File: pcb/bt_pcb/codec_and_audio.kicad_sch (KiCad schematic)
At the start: 10 parts, among them U1 CS4272

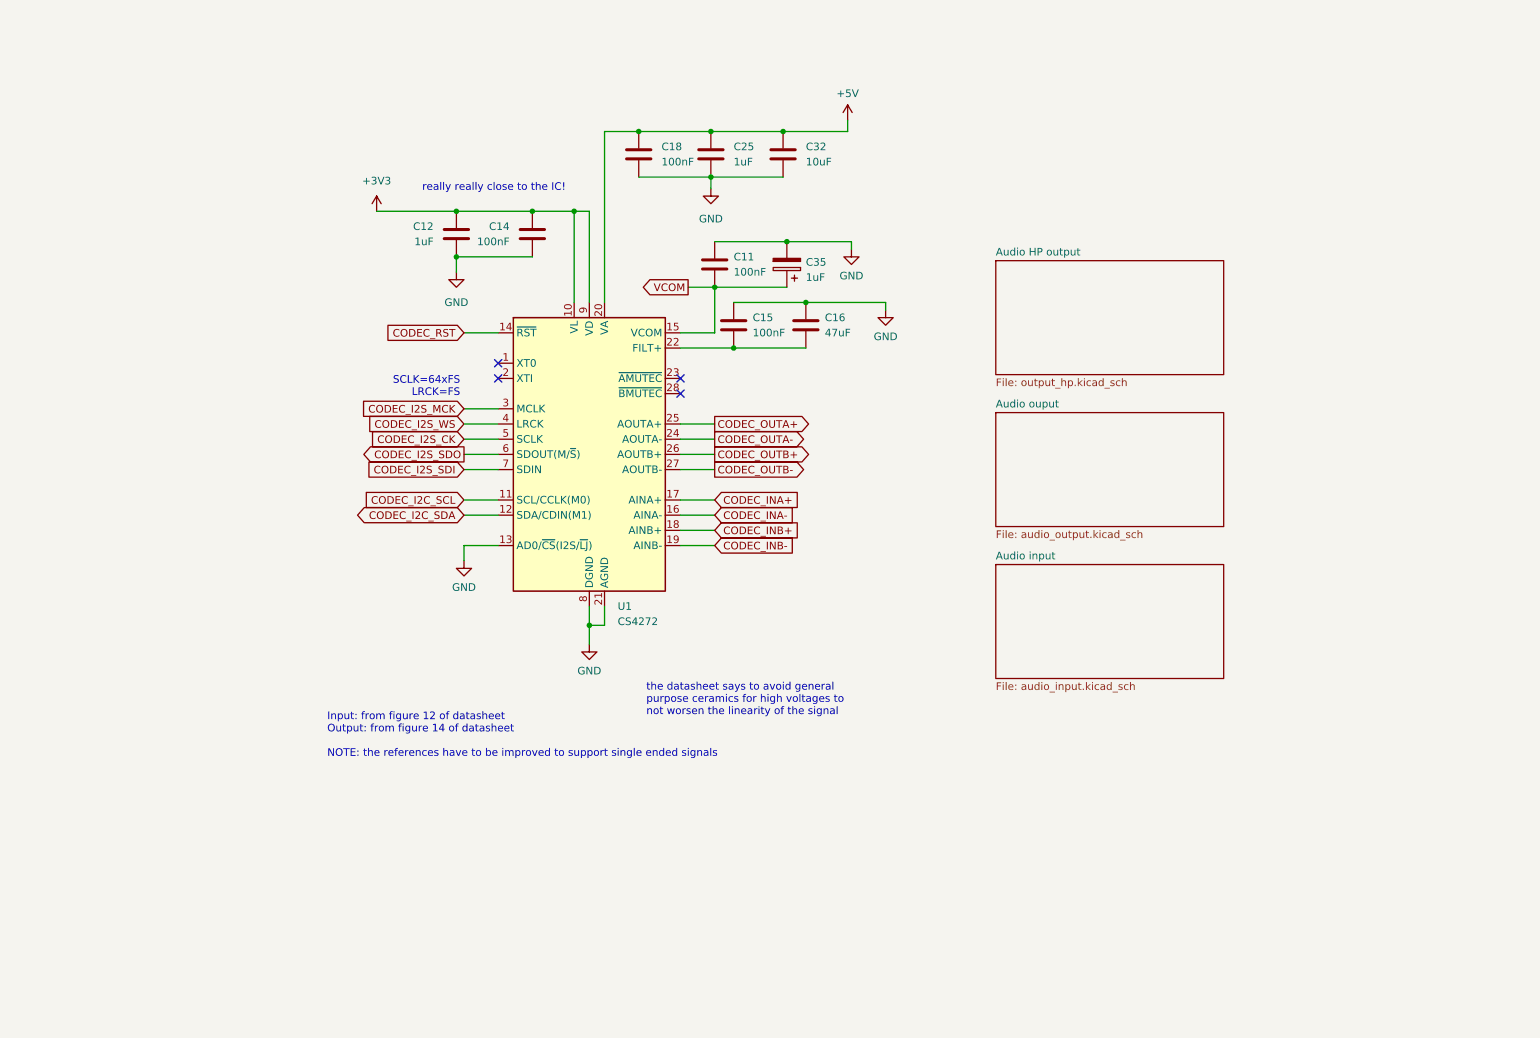
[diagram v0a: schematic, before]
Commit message: ditching power pcb, new codec
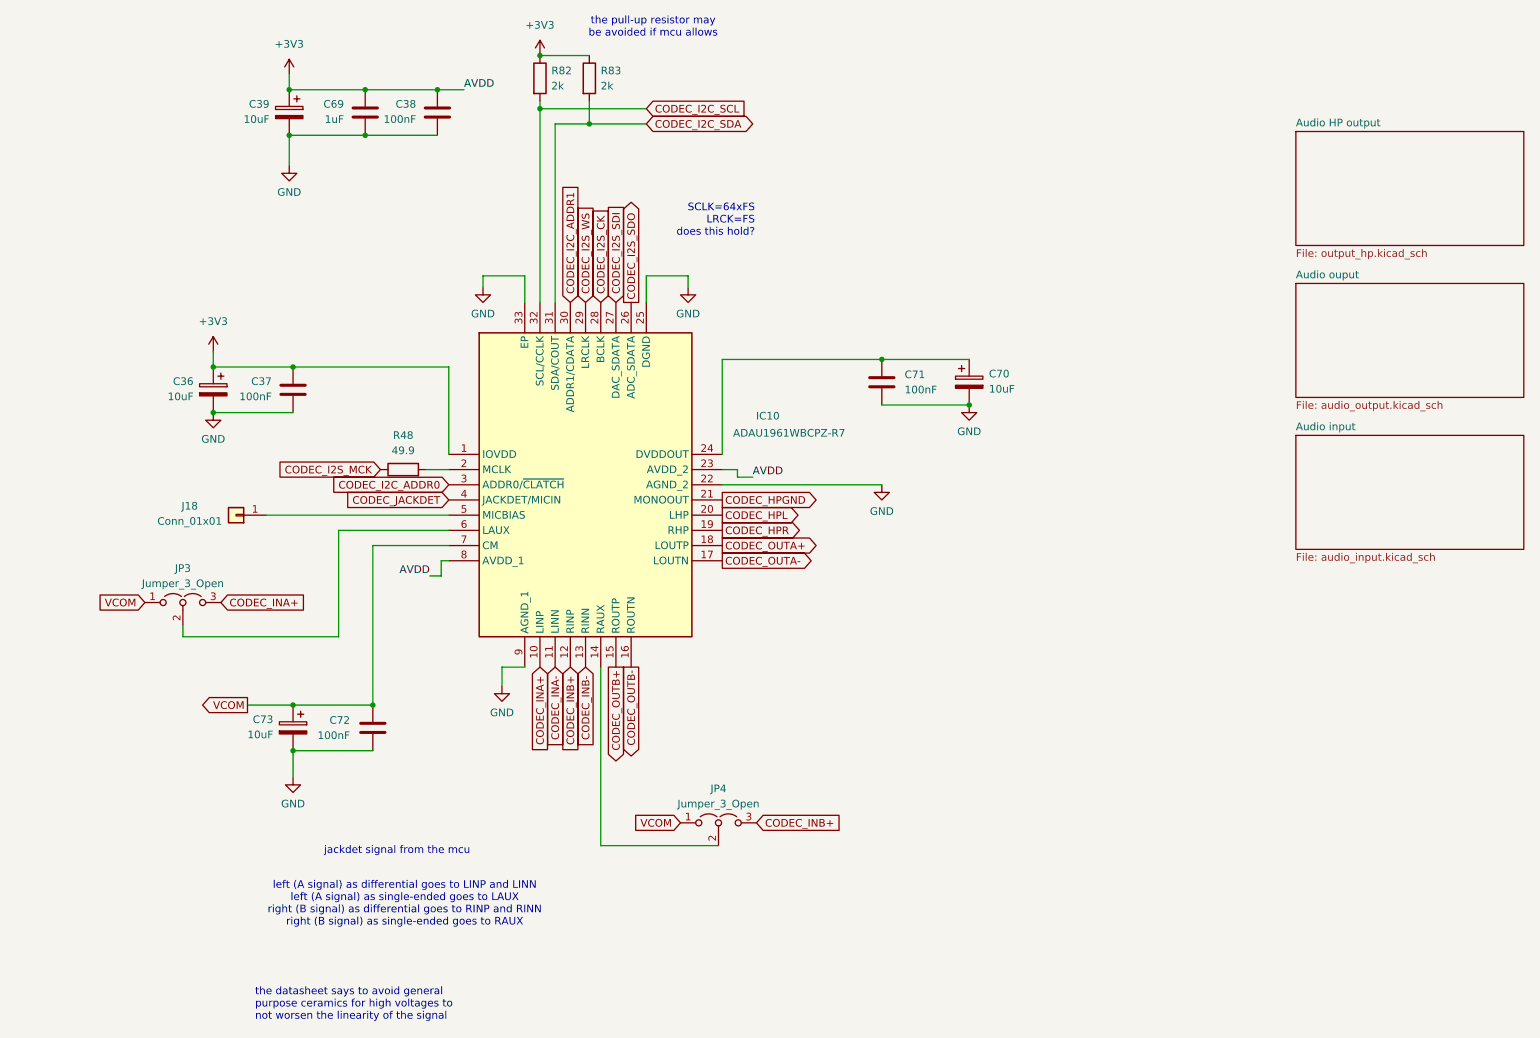
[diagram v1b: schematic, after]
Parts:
- removed C11, C14, C15, C18: 100nF, symbol Device:C
- removed C12, C25: 1uF, symbol Device:C
- removed C16: 47uF, symbol Device:C
- removed C32: 10uF, symbol Device:C
- removed C35: 1uF, symbol Device:C_Polarized
- removed U1: CS4272, Package_SO:TSSOP-28_4.4x9.7mm_P0.65mm, symbol Audio:CS4272
- added C36, C39, C70, C73: 10uF, symbol Device:C_Polarized
- added C37, C38, C71, C72: 100nF, symbol Device:C
- added C69: 1uF, symbol Device:C
- added IC10: ADAU1961WBCPZ-R7, QFN50P500X500X100-33N-D, symbol library:ADAU1961WBCPZ-R7
- added J18: Conn_01x01, symbol Connector_Generic:Conn_01x01
- added JP3, JP4: Jumper_3_Open, symbol Jumper:Jumper_3_Open
- added R48: 49.9, symbol Device:R
- added R82, R83: 2k, symbol Device:R
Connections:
- net +3V3: now also C36.1, C37.1, C38.1, C39.1, C69.1, IC10.1 (IOVDD), IC10.23 (AVDD_2), IC10.8 (AVDD_1), R82.1, R83.1
- net CODEC_I2C_SCL: now also IC10.32 (SCL/CCLK), R82.2
- net CODEC_I2C_SDA: now also IC10.31 (SDA/COUT), R83.2
- net CODEC_I2S_CK: now also IC10.28 (BCLK)
- net CODEC_I2S_MCK: now also R48.1
- net CODEC_I2S_SDI: now also IC10.27 (DAC_SDATA)
- net CODEC_I2S_SDO: now also IC10.26 (ADC_SDATA)
- net CODEC_I2S_WS: now also IC10.29 (LRCLK)
- net CODEC_INA+: now also IC10.10 (LINP), JP3.3 (B)
- net CODEC_INA-: now also IC10.11 (LINN)
- net CODEC_INB+: now also IC10.12 (RINP), JP4.3 (B)
- net CODEC_INB-: now also IC10.13 (RINN)
- net CODEC_OUTA+: now also IC10.18 (LOUTP)
- net CODEC_OUTA-: now also IC10.17 (LOUTN)
- net CODEC_OUTB+: now also IC10.15 (ROUTP)
- net CODEC_OUTB-: now also IC10.16 (ROUTN)
- net GND: now also C36.2, C37.2, C38.2, C39.2, C69.2, C70.2, C71.2, C72.2, C73.2, IC10.22 (AGND_2), IC10.25 (DGND), IC10.33 (EP), IC10.9 (AGND_1)
- net VCOM: now also C72.1, C73.1, IC10.7 (CM), JP3.1 (A), JP4.1 (A)
- new net: IC10.2 (MCLK), R48.2
- new net: IC10.14 (RAUX), JP4.2 (C)
- new net: C70.1, C71.1, IC10.24 (DVDDOUT)
- new net: IC10.5 (MICBIAS), J18.1 (Pin_1)
- new net: IC10.6 (LAUX), JP3.2 (C)
- new net CODEC_HPGND: IC10.21 (MONOOUT)
- new net CODEC_HPL: IC10.20 (LHP)
- new net CODEC_HPR: IC10.19 (RHP)
- new net CODEC_I2C_ADDR0: IC10.3 (ADDR0/~{CLATCH})
- new net CODEC_I2C_ADDR1: IC10.30 (ADDR1/CDATA)
- new net CODEC_JACKDET: IC10.4 (JACKDET/MICIN)
- no-connect marks 4 -> 0
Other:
- note added: "SCLK=64xFS LRCK=FS does this hold?"
- note added: "jackdet signal from the mcu"
- note added: "left (A signal) as differential goes to LINP and LINN left (A signal) as single-ended goes to LAUX right (B signal) as differential goes to RINP and RINN right (B signal) as single-ended goes to RAUX"
- note added: "the pull-up resistor may be avoided if mcu allows"
- note removed: "Input: from figure 12 of datasheet Output: from figure 14 of datasheet NOTE: the references have to be improved to support single ended signals"
- note removed: "SCLK=64xFS LRCK=FS"
- note removed: "really really close to the IC!"

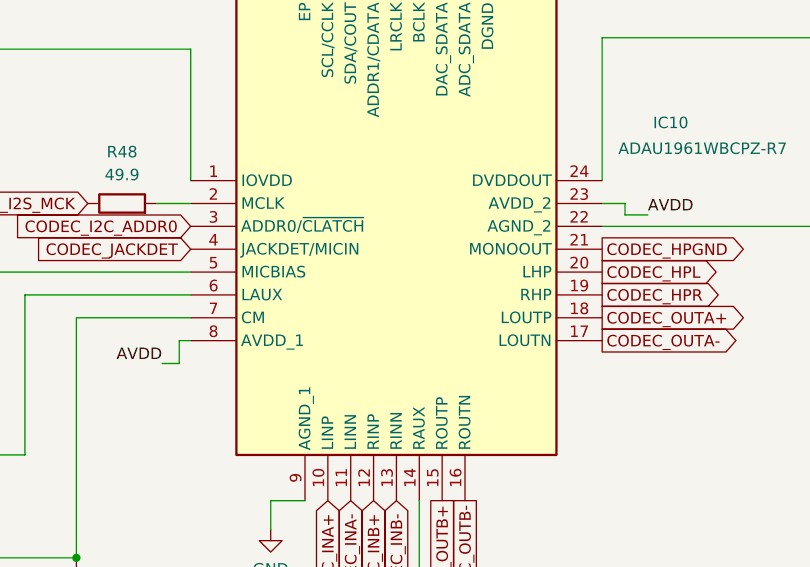
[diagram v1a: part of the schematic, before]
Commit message: complete makeover of power supply
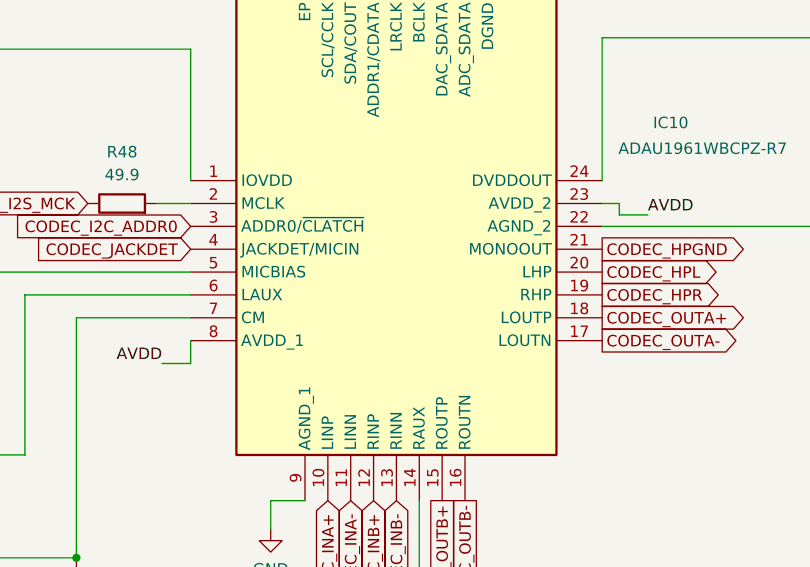
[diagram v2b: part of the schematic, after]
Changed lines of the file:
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@@
 	(wire
 		(pts
-			(xy 98.425 114.3) (xy 100.33 114.3)
+			(xy 98.425 114.3) (xy 101.6 114.3)
 		)
 		(stroke
@@
 	(wire
 		(pts
-			(xy 100.33 114.3) (xy 100.33 111.76)
-		)
-		(stroke
-			(width 0)
-			(type default)
-		)
-	)
-	(wire
-		(pts
-			(xy 100.33 111.76) (xy 101.6 111.76)
+			(xy 101.6 114.3) (xy 101.6 111.76)
 		)
 		(stroke
@@
 	(wire
 		(pts
-			(xy 152.4 97.79) (xy 149.86 97.79)
+			(xy 152.4 97.79) (xy 149.225 97.79)
 		)
 		(stroke
@@
 	(wire
 		(pts
-			(xy 149.86 96.52) (xy 147.32 96.52)
+			(xy 149.225 96.52) (xy 147.32 96.52)
 		)
 		(stroke
@@
 	(wire
 		(pts
-			(xy 149.86 97.79) (xy 149.86 96.52)
-		)
-		(stroke
+			(xy 149.225 97.79) (xy 149.225 96.52)
+		)
+		(stroke

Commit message: big progress, now revising error and warnings
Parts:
- removed C36, C39, C70, C73: 10uF, symbol Device:C_Polarized
- removed R82, R83: 2k, symbol Device:R
- added C3, C4, C5, C6: 10uF, symbol Device:C
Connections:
- net +3V3: now also C5.1; no longer C38.1, C69.1, IC10.23 (AVDD_2), IC10.8 (AVDD_1)
- net GND: now also C3.2, C4.2, C5.2, C6.2
- net VCOM: now also C6.1
- net at C71.1, IC10.24 (DVDDOUT): now also C3.1
- new net +3V3A: C38.1, C4.1, C69.1, IC10.23 (AVDD_2), IC10.8 (AVDD_1)
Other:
- note removed: "the pull-up resistor may be avoided if mcu allows"

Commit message: solving some erc warnings and errors
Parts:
- IC2: renamed from IC10; footprint QFN50P500X500X100-33N-D -> library:QFN50P500X500X100-33N-D
- renumbered C5 to C15, C4 to C16, C37 to C17, C6 to C18, C69 to C19, C72 to C20, C38 to C21, C71 to C22, C3 to C23, J18 to J3, JP3 to JP1, JP4 to JP2, R48 to R2
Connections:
- net +3V3A renamed +3.3VA
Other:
- moved on the sheet: C15, C17, C18, C21, C22, C23, JP1, JP2

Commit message: schematic in theory finished
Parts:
- removed JP1, JP2: Jumper_3_Open, symbol Jumper:Jumper_3_Open
- added J4: Conn_01x03, Connector_PinHeader_2.54mm:PinHeader_1x01_P2.54mm_Vertical, symbol Connector_Generic:Conn_01x03
- added R3, R4, R5, R6: 0, Resistor_SMD:R_0603_1608Metric_Pad0.98x0.95mm_HandSolder, symbol Device:R
- C15: renamed from C16; value 10uF -> 10u; footprint (none) -> Capacitor_SMD:C_0805_2012Metric_Pad1.18x1.45mm_HandSolder
- C16: renamed from C19; value 1uF -> 1u; footprint (none) -> Capacitor_SMD:C_0603_1608Metric_Pad1.08x0.95mm_HandSolder
- C17: renamed from C21; value 100nF -> 100n; footprint (none) -> Capacitor_SMD:C_0603_1608Metric_Pad1.08x0.95mm_HandSolder
- C18: renamed from C22; value 100nF -> 100n; footprint (none) -> Capacitor_SMD:C_0603_1608Metric_Pad1.08x0.95mm_HandSolder
- C19: renamed from C23; value 10uF -> 10u; footprint (none) -> Capacitor_SMD:C_0805_2012Metric_Pad1.18x1.45mm_HandSolder
- C20: renamed from C15; value 10uF -> 10u; footprint (none) -> Capacitor_SMD:C_0805_2012Metric_Pad1.18x1.45mm_HandSolder
- C21: renamed from C17; value 100nF -> 100n; footprint (none) -> Capacitor_SMD:C_0603_1608Metric_Pad1.08x0.95mm_HandSolder
- C22: renamed from C18; value 10uF -> 10u; footprint (none) -> Capacitor_SMD:C_0805_2012Metric_Pad1.18x1.45mm_HandSolder
- C23: renamed from C20; value 100nF -> 100n; footprint (none) -> Capacitor_SMD:C_0603_1608Metric_Pad1.08x0.95mm_HandSolder
- J3: footprint (none) -> Connector_PinHeader_2.54mm:PinHeader_1x01_P2.54mm_Vertical
- R2: footprint (none) -> Resistor_SMD:R_0603_1608Metric_Pad0.98x0.95mm_HandSolder
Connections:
- net CODEC_HPGND: now also J4.3 (Pin_3)
- net CODEC_HPL: now also J4.1 (Pin_1)
- net CODEC_HPR: now also J4.2 (Pin_2)
- net CODEC_INA+: now also R4.2
- net CODEC_INB+: now also R6.2
- net VCOM: now also R3.1, R5.1
- net at IC2.14 (RAUX): now also R5.2, R6.1
- net at IC2.6 (LAUX): now also R3.2, R4.1
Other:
- removed sheet Audio HP output
- note added: "HEADPHONE OUT Left -> 1 -> T Right -> 2 -> R Ggn -> 3 -> S"

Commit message: pcb started
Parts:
- J5: renamed from J4; footprint Connector_PinHeader_2.54mm:PinHeader_1x01_P2.54mm_Vertical -> Connector_PinHeader_2.54mm:PinHeader_1x03_P2.54mm_Vertical
- renumbered J3 to J4, R2 to R3, R3 to R4, R4 to R5, R5 to R6, R6 to R7
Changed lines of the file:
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@@
 		(dnp no)
 		(fields_autoplaced yes)
-		(property "Reference" "#PWR018"
+		(property "Reference" "#PWR019"
 			(at 62.23 81.28 0)
 			(effects
@@
 			(project ""
 				(path "/eb787481-08cd-41a4-a128-173fa6227c32/4ada0139-8712-47ce-9d4c-ab8fef312f7b"
-					(reference "#PWR018")
+					(reference "#PWR019")
 					(unit 1)
 				)
@@
 		(dnp no)
 		(fields_autoplaced yes)
-		(property "Reference" "#PWR016"
+		(property "Reference" "#PWR017"
 			(at 107.95 72.39 0)
 			(effects
@@
 			(project "bt_pcb"
 				(path "/eb787481-08cd-41a4-a128-173fa6227c32/4ada0139-8712-47ce-9d4c-ab8fef312f7b"
-					(reference "#PWR016")
+					(reference "#PWR017")
 					(unit 1)
 				)
@@
 		(dnp no)
 		(fields_autoplaced yes)
-		(property "Reference" "R3"
+		(property "Reference" "R4"
 			(at 53.34 113.665 90)
 			(effects
@@
 			(project "bt_pcb"
 				(path "/eb787481-08cd-41a4-a128-173fa6227c32/4ada0139-8712-47ce-9d4c-ab8fef312f7b"
-					(reference "R3")
+					(reference "R4")
 					(unit 1)
 				)
@@
 		(dnp no)
 		(fields_autoplaced yes)
-		(property "Reference" "R5"
+		(property "Reference" "R6"
 			(at 143.51 150.495 90)
 			(effects
@@
 			(project "bt_pcb"
 				(path "/eb787481-08cd-41a4-a128-173fa6227c32/4ada0139-8712-47ce-9d4c-ab8fef312f7b"
-					(reference "R5")
+					(reference "R6")
 					(unit 1)
 				)
@@
 		(dnp no)
 		(fields_autoplaced yes)
-		(property "Reference" "#PWR019"
+		(property "Reference" "#PWR020"
 			(at 189.23 92.71 0)
 			(effects
@@
 			(project "bt_pcb"
 				(path "/eb787481-08cd-41a4-a128-173fa6227c32/4ada0139-8712-47ce-9d4c-ab8fef312f7b"
-					(reference "#PWR019")
+					(reference "#PWR020")
 					(unit 1)
 				)
@@
 		(dnp no)
 		(fields_autoplaced yes)
-		(property "Reference" "#PWR022"
+		(property "Reference" "#PWR023"
 			(at 110.49 139.7 0)
 			(effects
@@
 			(project "bt_pcb"
 				(path "/eb787481-08cd-41a4-a128-173fa6227c32/4ada0139-8712-47ce-9d4c-ab8fef312f7b"
-					(reference "#PWR022")
+					(reference "#PWR023")
 					(unit 1)
 				)
@@
 		(dnp no)
 		(fields_autoplaced yes)
-		(property "Reference" "R2"
+		(property "Reference" "R3"
 			(at 93.98 90.805 90)
 			(effects
@@
 			(project ""
 				(path "/eb787481-08cd-41a4-a128-173fa6227c32/4ada0139-8712-47ce-9d4c-ab8fef312f7b"
-					(reference "R2")
+					(reference "R3")
 					(unit 1)
 				)
@@
 		(dnp no)
 		(fields_autoplaced yes)
-		(property "Reference" "#PWR020"
+		(property "Reference" "#PWR021"
 			(at 62.23 93.98 0)
 			(effects
@@
 			(project "bt_pcb"
 				(path "/eb787481-08cd-41a4-a128-173fa6227c32/4ada0139-8712-47ce-9d4c-ab8fef312f7b"
-					(reference "#PWR020")
+					(reference "#PWR021")
 					(unit 1)
 				)
@@
 		(dnp no)
 		(fields_autoplaced yes)
-		(property "Reference" "#PWR014"
+		(property "Reference" "#PWR015"
 			(at 74.93 34.29 0)
 			(effects
@@
 			(project ""
 				(path "/eb787481-08cd-41a4-a128-173fa6227c32/4ada0139-8712-47ce-9d4c-ab8fef312f7b"
-					(reference "#PWR014")
+					(reference "#PWR015")
 					(unit 1)
 				)
@@
 		(dnp no)
 		(fields_autoplaced yes)
-		(property "Reference" "#PWR023"
+		(property "Reference" "#PWR024"
 			(at 76.2 154.94 0)
 			(effects
@@
 			(project "bt_pcb"
 				(path "/eb787481-08cd-41a4-a128-173fa6227c32/4ada0139-8712-47ce-9d4c-ab8fef312f7b"
-					(reference "#PWR023")
+					(reference "#PWR024")
 					(unit 1)
 				)
@@
 		(dnp no)
 		(fields_autoplaced yes)
-		(property "Reference" "J4"
+		(property "Reference" "J5"
 			(at 262.255 134.6199 0)
 			(effects
@@
 			)
 		)
-		(property "Footprint" "Connector_PinHeader_2.54mm:PinHeader_1x01_P2.54mm_Vertical"
+		(property "Footprint" "Connector_PinHeader_2.54mm:PinHeader_1x03_P2.54mm_Vertical"
 			(at 259.08 135.89 0)
 			(effects
@@
 			(project "bt_pcb"
 				(path "/eb787481-08cd-41a4-a128-173fa6227c32/4ada0139-8712-47ce-9d4c-ab8fef312f7b"
-					(reference "J4")
+					(reference "J5")
 					(unit 1)
 				)
@@
 		(dnp no)
 		(fields_autoplaced yes)
-		(property "Reference" "R6"
+		(property "Reference" "R7"
 			(at 151.13 150.495 90)
 			(effects
@@
 			(project "bt_pcb"
 				(path "/eb787481-08cd-41a4-a128-173fa6227c32/4ada0139-8712-47ce-9d4c-ab8fef312f7b"
-					(reference "R6")
+					(reference "R7")
 					(unit 1)
 				)
@@
 		(dnp no)
 		(fields_autoplaced yes)
-		(property "Reference" "R4"
+		(property "Reference" "R5"
 			(at 60.96 113.665 90)
 			(effects
@@
 			(project "bt_pcb"
 				(path "/eb787481-08cd-41a4-a128-173fa6227c32/4ada0139-8712-47ce-9d4c-ab8fef312f7b"
-					(reference "R4")
+					(reference "R5")
 					(unit 1)
 				)
@@
 		(dnp no)
 		(fields_autoplaced yes)
-		(property "Reference" "#PWR015"
+		(property "Reference" "#PWR016"
 			(at 74.93 52.07 0)
 			(effects
@@
 			(project "bt_pcb"
 				(path "/eb787481-08cd-41a4-a128-173fa6227c32/4ada0139-8712-47ce-9d4c-ab8fef312f7b"
-					(reference "#PWR015")
+					(reference "#PWR016")
 					(unit 1)
 				)
@@
 		(on_board yes)
 		(dnp no)
-		(property "Reference" "J3"
+		(property "Reference" "J4"
 			(at 58.293 102.616 0)
 			(effects
@@
 			(project "bt_pcb"
 				(path "/eb787481-08cd-41a4-a128-173fa6227c32/4ada0139-8712-47ce-9d4c-ab8fef312f7b"
-					(reference "J3")
+					(reference "J4")
 					(unit 1)
 				)
@@
 		(dnp no)
 		(fields_autoplaced yes)
-		(property "Reference" "#PWR017"
+		(property "Reference" "#PWR018"
 			(at 142.24 72.39 0)
 			(effects
@@
 			(project "bt_pcb"
 				(path "/eb787481-08cd-41a4-a128-173fa6227c32/4ada0139-8712-47ce-9d4c-ab8fef312f7b"
-					(reference "#PWR017")
+					(reference "#PWR018")
 					(unit 1)
 				)
@@
 		(dnp no)
 		(fields_autoplaced yes)
-		(property "Reference" "#PWR021"
+		(property "Reference" "#PWR022"
 			(at 173.99 105.41 0)
 			(effects
@@
 			(project "bt_pcb"
 				(path "/eb787481-08cd-41a4-a128-173fa6227c32/4ada0139-8712-47ce-9d4c-ab8fef312f7b"
-					(reference "#PWR021")
-					(unit 1)
-				)
+					(reference "#PWR022")
+					(unit 1)
+				)
